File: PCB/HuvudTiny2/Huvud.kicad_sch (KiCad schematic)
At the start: 97 parts, among them J1 Vin, J12 USB_Micro-B, J2 DBG, J3 THERM, J4 FAN0, J5 FAN1, J6 Heater, J7 Endstop, J9 STEPPER, Q1 AO3400A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

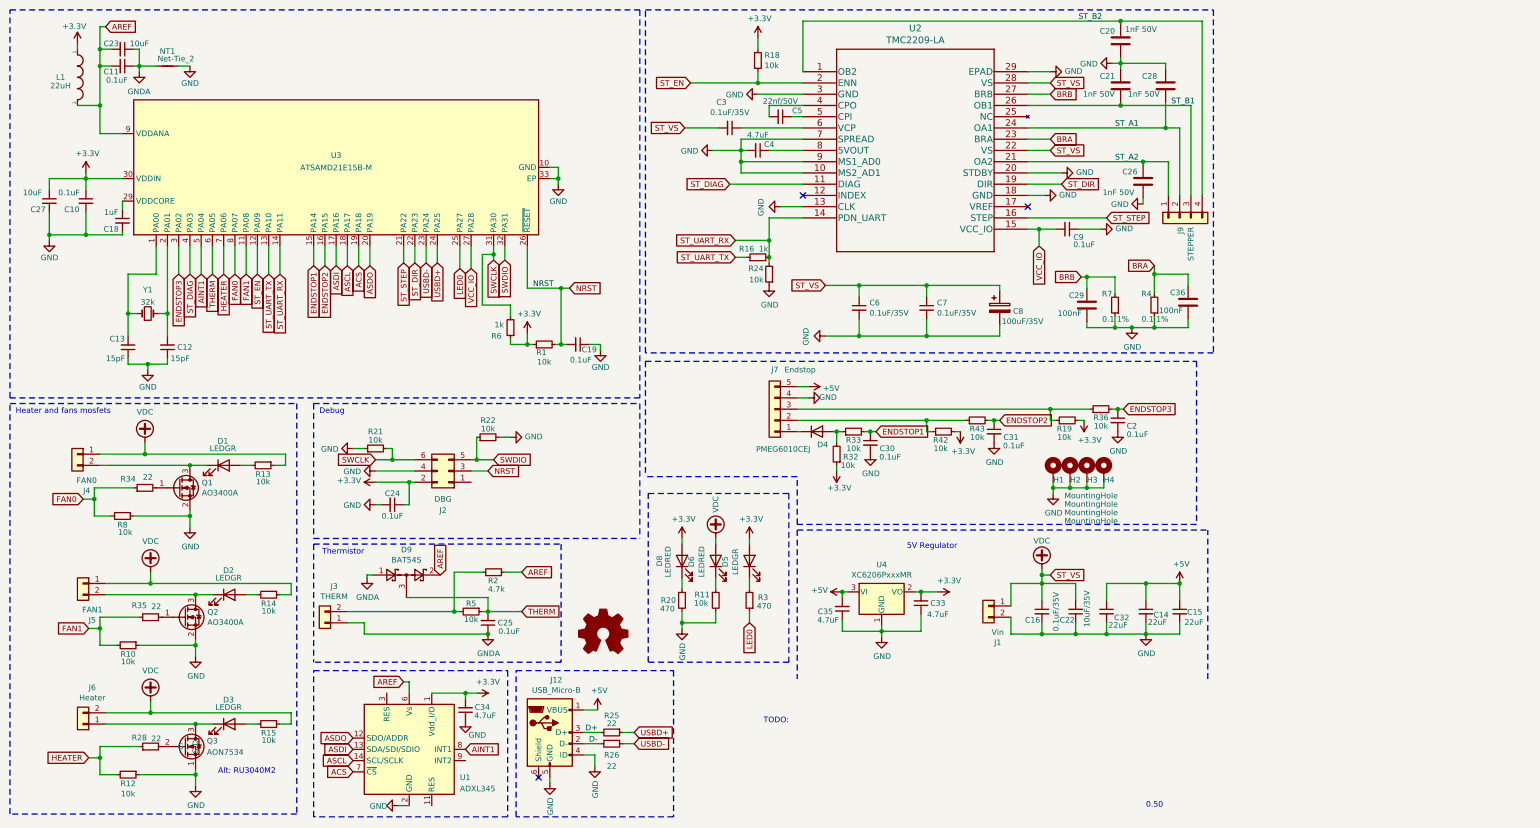
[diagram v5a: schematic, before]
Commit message: Flipped FAN connectors. Changed pinout on endstop connector. Added SPI thermocouple connector - shared CS with THERMISTOR.
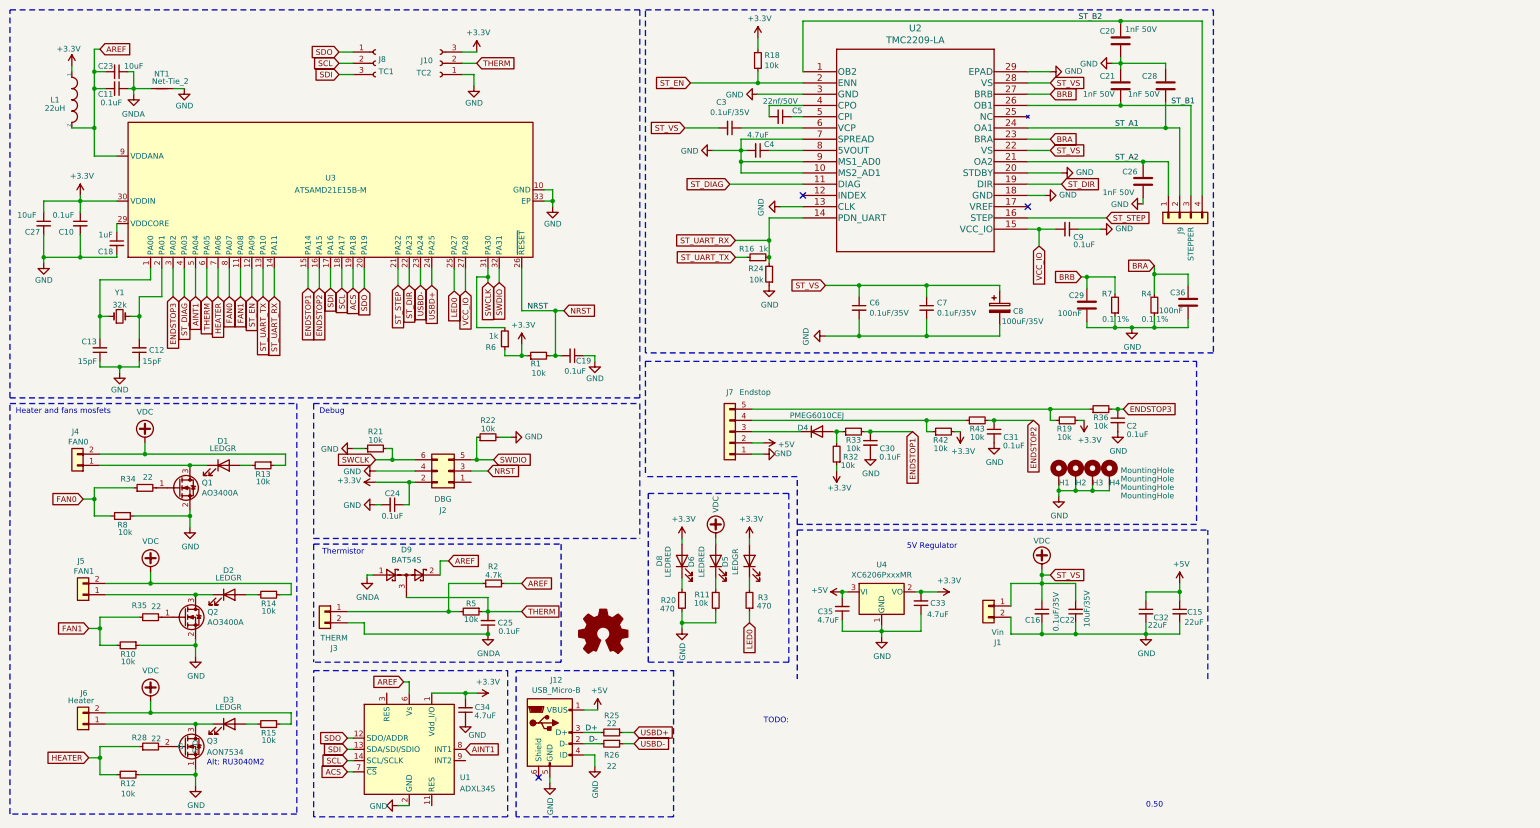
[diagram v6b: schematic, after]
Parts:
- removed C14: 22uF, Capacitor_SMD:C_0805_2012Metric, symbol Device:C_Small
- added J10: TC2, Connector_PinHeader_1.27mm:PinHeader_1x03_P1.27mm_Vertical, symbol Connector:Conn_01x03_Female
- added J8: TC1, Connector_PinSocket_1.27mm:PinSocket_1x03_P1.27mm_Vertical, symbol Connector:Conn_01x03_Female
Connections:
- net +3V3: now also J10.3 (Pin_3)
- net +5V: now also J7.2 (Pin_2); no longer J7.5 (Pin_5)
- net GND: now also J7.1 (Pin_1), J10.1 (Pin_1); no longer J7.4 (Pin_4)
- net GNDA: now also J3.2 (Pin_2); no longer J3.1 (Pin_1)
- net THERM: now also J10.2 (Pin_2)
- net VDC: now also J4.2 (Pin_2), J5.2 (Pin_2); no longer J4.1 (Pin_1), J5.1 (Pin_1)
- net at D1.1 (K), Q1.3 (D): now also J4.1 (Pin_1); no longer J4.2 (Pin_2)
- net at D2.1 (K), Q2.3 (D): now also J5.1 (Pin_1); no longer J5.2 (Pin_2)
- net at R2.1, R5.2: now also J3.1 (Pin_1); no longer J3.2 (Pin_2)
- net at D4.1 (K): now also J7.3 (Pin_3); no longer J7.1 (Pin_1)
- net at R42.1, R43.1: now also J7.4 (Pin_4); no longer J7.2 (Pin_2)
- net at R19.1, R36.1: now also J7.5 (Pin_5); no longer J7.3 (Pin_3)
- net ASCL renamed SCL
- net SCL: now also J8.2 (Pin_2)
- net ASDI renamed SDI
- net SDI: now also J8.3 (Pin_3)
- net ASDO renamed SDO
- net SDO: now also J8.1 (Pin_1)
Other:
- moved on the sheet: C10, C11, C12, C13, C18, C19, C23, C27, C32, H1, H2, H3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

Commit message: Route new version with 1.25mm connectors. Added TH2 and 24V on the endstop connector.
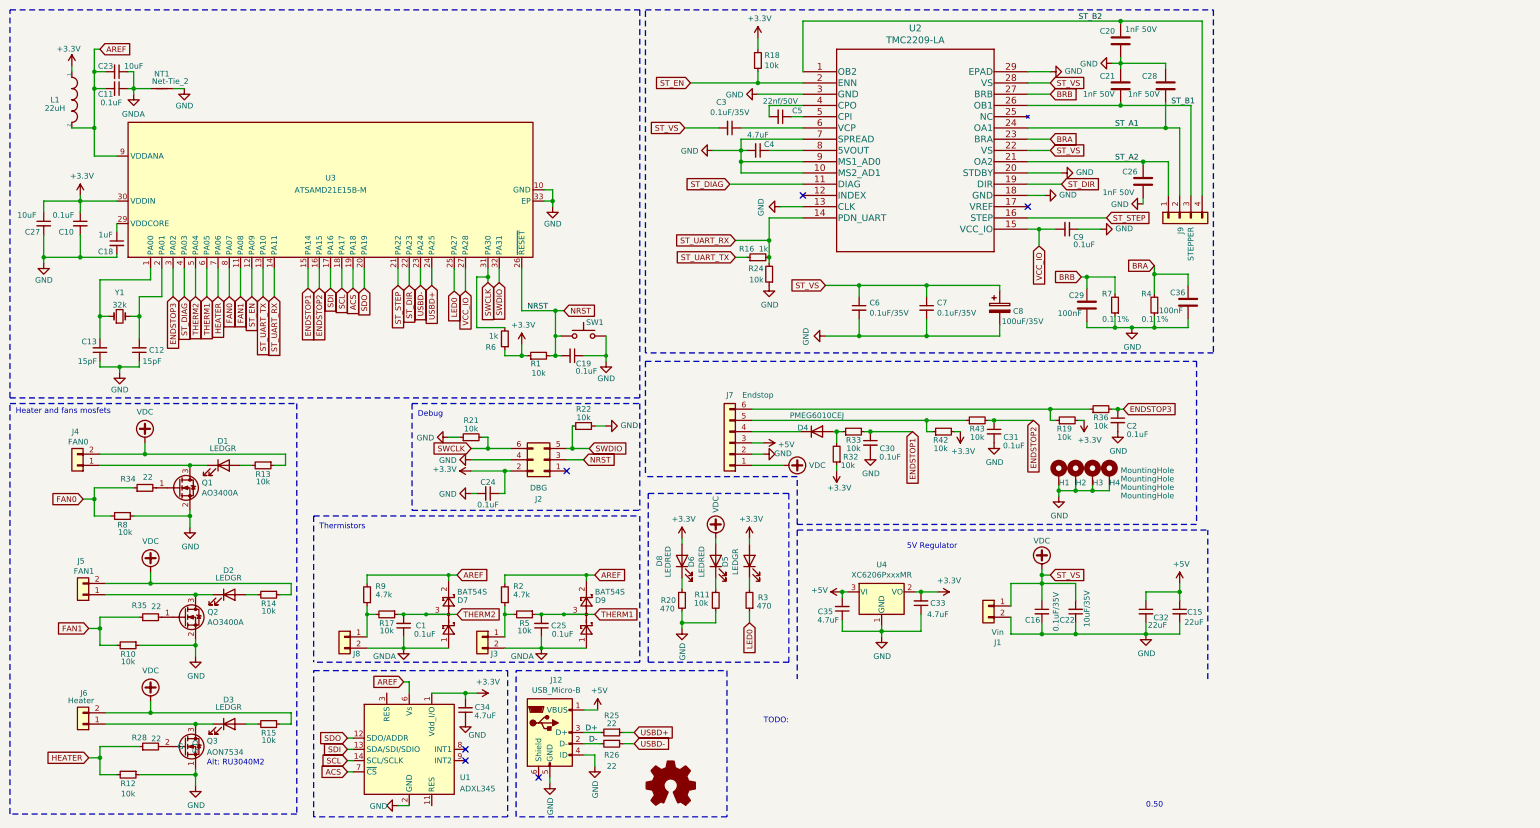
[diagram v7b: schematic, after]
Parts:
- removed J10: TC2, Connector_PinHeader_1.27mm:PinHeader_1x03_P1.27mm_Vertical, symbol Connector:Conn_01x03_Female
- removed J8: TC1, Connector_PinSocket_1.27mm:PinSocket_1x03_P1.27mm_Vertical, symbol Connector:Conn_01x03_Female
- added C1: 0.1uF, Capacitor_SMD:C_0402_1005Metric, symbol Device:C_Small
- added D7: BAT54S, Package_TO_SOT_SMD:SOT-23, symbol Diode:BAT54S
- added J8: THERM, Connector_Hirose:Hirose_DF13-02P-1.25DSA_1x02_P1.25mm_Vertical, symbol Connector_Generic:Conn_01x02
- added R17: 10k, Resistor_SMD:R_0402_1005Metric, symbol Device:R_Small
- added R9: 4.7k, Resistor_SMD:R_0402_1005Metric, symbol Device:R_Small
- added SW1: SW_Push, Button_Switch_SMD:SW_SPST_EVQP2, symbol Switch:SW_Push
- J2: footprint Connector_PinHeader_2.54mm:PinHeader_2x03_P2.54mm_Vertical -> Connector_PinHeader_1.27mm:PinHeader_2x03_P1.27mm_Vertical; LCSC C402781 -> (none)
- J3, J4, J5: footprint Connector_JST:JST_PH_B2B-PH-K_1x02_P2.00mm_Vertical -> Connector_Hirose:Hirose_DF13-02P-1.25DSA_1x02_P1.25mm_Vertical; LCSC C225188 -> C506675
- J7: footprint Connector_JST:JST_PH_B5B-PH-K_1x05_P2.00mm_Vertical -> Connector_Hirose:Hirose_DF13-06P-1.25DSA_1x06_P1.25mm_Vertical; symbol Connector_Generic:Conn_01x05 -> Connector_Generic:Conn_01x06; LCSC C225191 -> C530977
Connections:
- net +5V: now also J7.3 (Pin_3); no longer J7.2 (Pin_2)
- net AREF: now also D7.2, R9.2
- net GND: now also J7.2 (Pin_2), SW1.2; no longer J7.1 (Pin_1)
- net GNDA: now also C1.1, D7.1, J8.2 (Pin_2)
- net NRST: now also SW1.1
- net VDC: now also J7.1 (Pin_1)
- net at D4.1 (K): now also J7.4 (Pin_4); no longer J7.3 (Pin_3)
- net at R42.1, R43.1: now also J7.5 (Pin_5); no longer J7.4 (Pin_4)
- net at R19.1, R36.1: now also J7.6 (Pin_6); no longer J7.5 (Pin_5)
- net AINT1: no longer names the net of U1.8 (INT1)
- net AINT1: no longer U3.5 (PA04)
- net THERM renamed THERM1
- new net: J8.1 (Pin_1), R17.2, R9.1
- new net THERM2: C1.2, D7.3, R17.1, U3.5 (PA04)
- no-connect marks 3 -> 6
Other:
- note added: "Thermistors"
- note removed: "Thermistor"
- moved on the sheet: C24, C25, D9, J2, J3, R2, R21, R22, R5

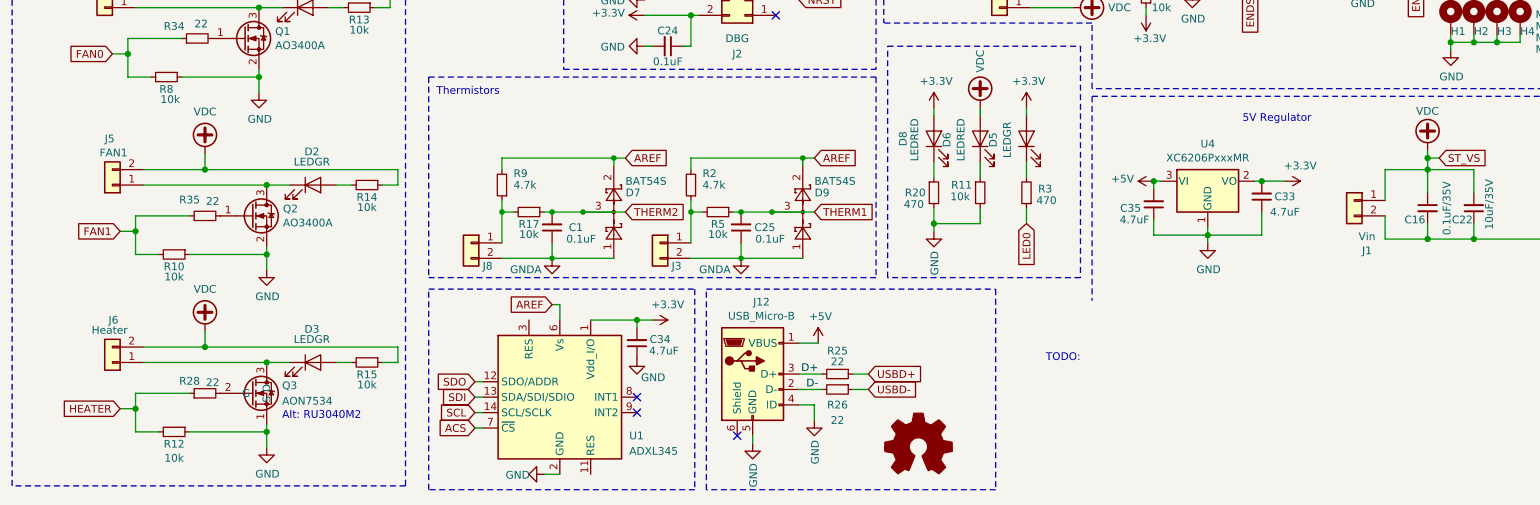
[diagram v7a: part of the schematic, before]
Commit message: Switched power & USB to MOLEX MicroFit 2x6. Switched heater to 3.5mm terminal.
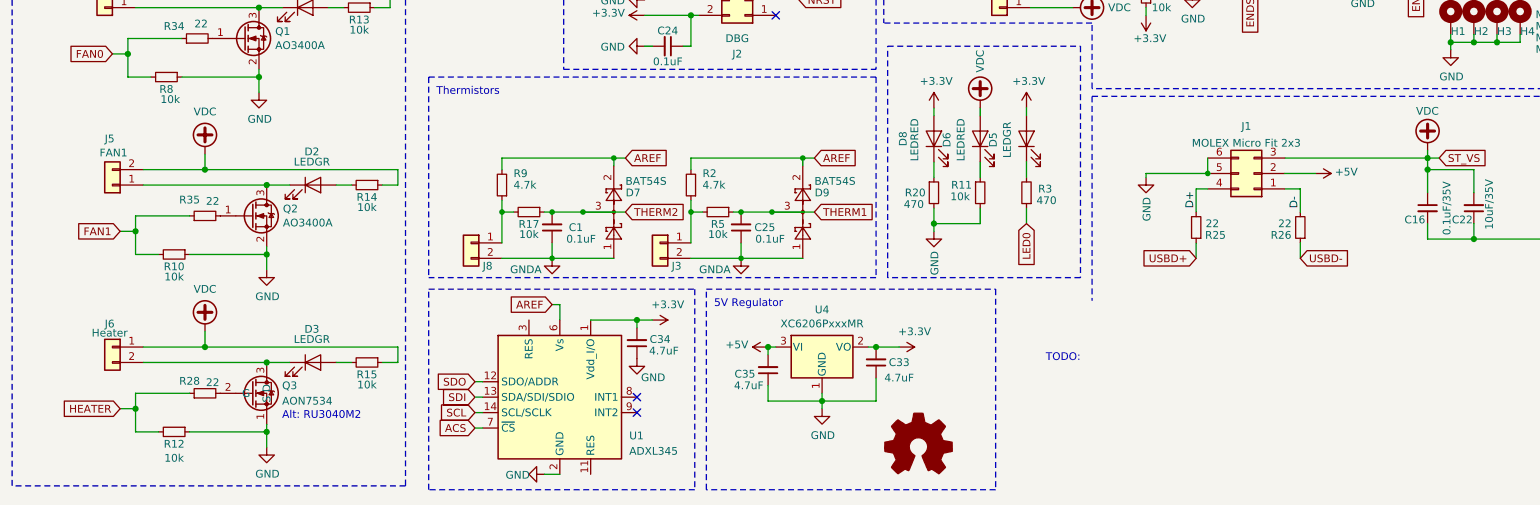
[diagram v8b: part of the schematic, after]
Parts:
- removed J1: Vin, Huvud:TerminalBlock_TE_282834-2_1x02_P2.54mm_Horizontal, symbol Connector_Generic:Conn_01x02
- removed J12: USB_Micro-B, Huvud:MC-101C, symbol Connector:USB_B_Micro
- added J1: MOLEX Micro Fit 2x3, Connector_Molex:Molex_Micro-Fit_3.0_43045-0600_2x03_P3.00mm_Horizontal, symbol Connector_Generic:Conn_02x03_Top_Bottom
- J6: footprint Huvud:TerminalBlock_TE_282834-2_1x02_P2.54mm_Horizontal -> Huvud:TerminalBlock_Phoenix_PT-1,5-2-3.5-H_1x02_P3.50mm_Horizontal
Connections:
- net +5V: now also J1.2 (Pin_2)
- net D+: now also J1.4 (Pin_4)
- net D-: now also J1.1 (Pin_1)
- net GND: now also J1.5 (Pin_5), J1.6 (Pin_6)
- net VDC: now also J6.1 (Pin_1), J1.3 (Pin_3); no longer J6.2 (Pin_2)
- net at D3.1 (K), Q3.3 (D): now also J6.2 (Pin_2); no longer J6.1 (Pin_1)
- no-connect marks 6 -> 5
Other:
- moved on the sheet: C33, C35, J6, R25, R26, U4
